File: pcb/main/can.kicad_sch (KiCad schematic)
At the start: 3 parts, among them J10 Conn, J8 Conn, J9 Conn

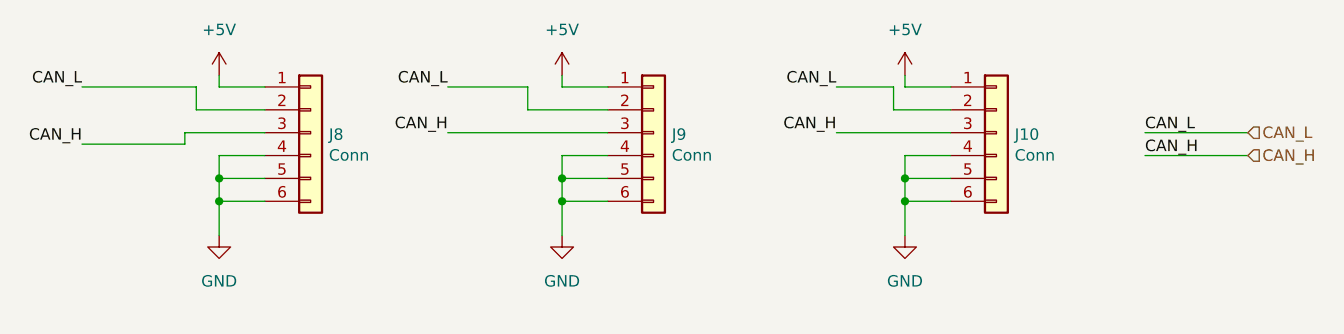
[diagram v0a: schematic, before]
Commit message: feat: delete two CAN connectors & add microSD input pin
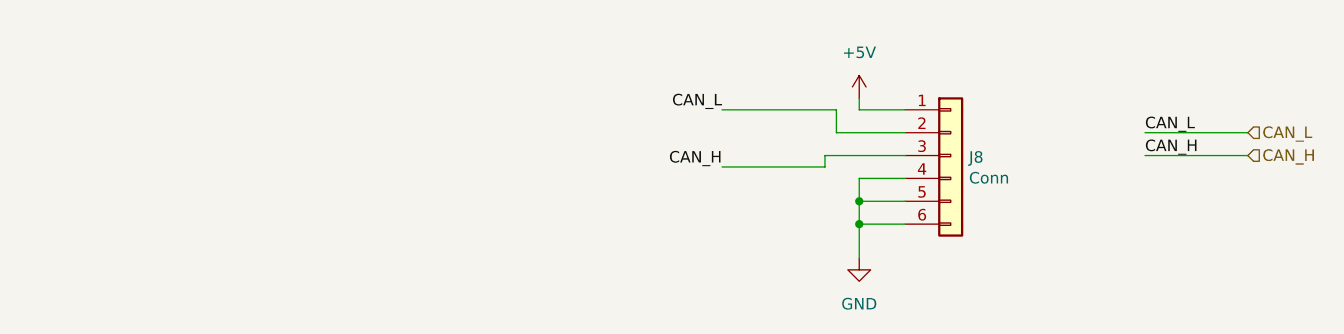
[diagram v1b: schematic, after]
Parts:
- removed J10, J9: Conn, bldc_lib:21322604YY, symbol Connector_Generic:Conn_01x06
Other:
- moved on the sheet: J8
